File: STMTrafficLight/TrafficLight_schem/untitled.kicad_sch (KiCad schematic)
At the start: 25 parts, among them U1 74HC595D, U2 74HC595D, U3 74HC595D

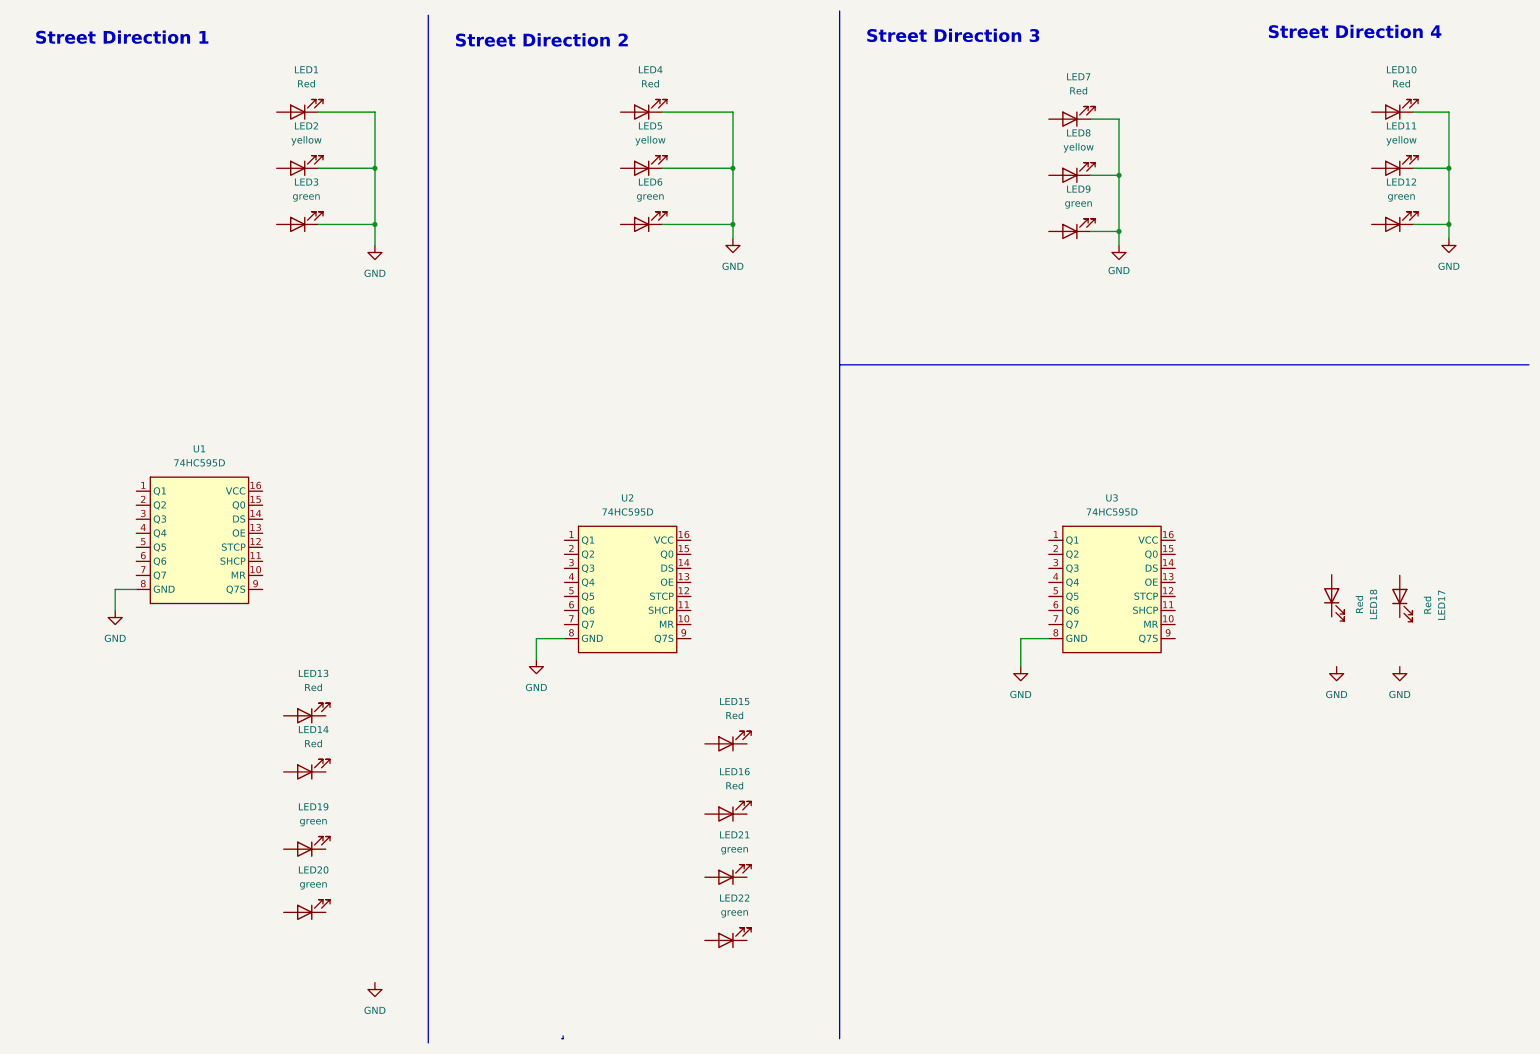
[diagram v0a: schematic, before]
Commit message: started on the traffic light shield
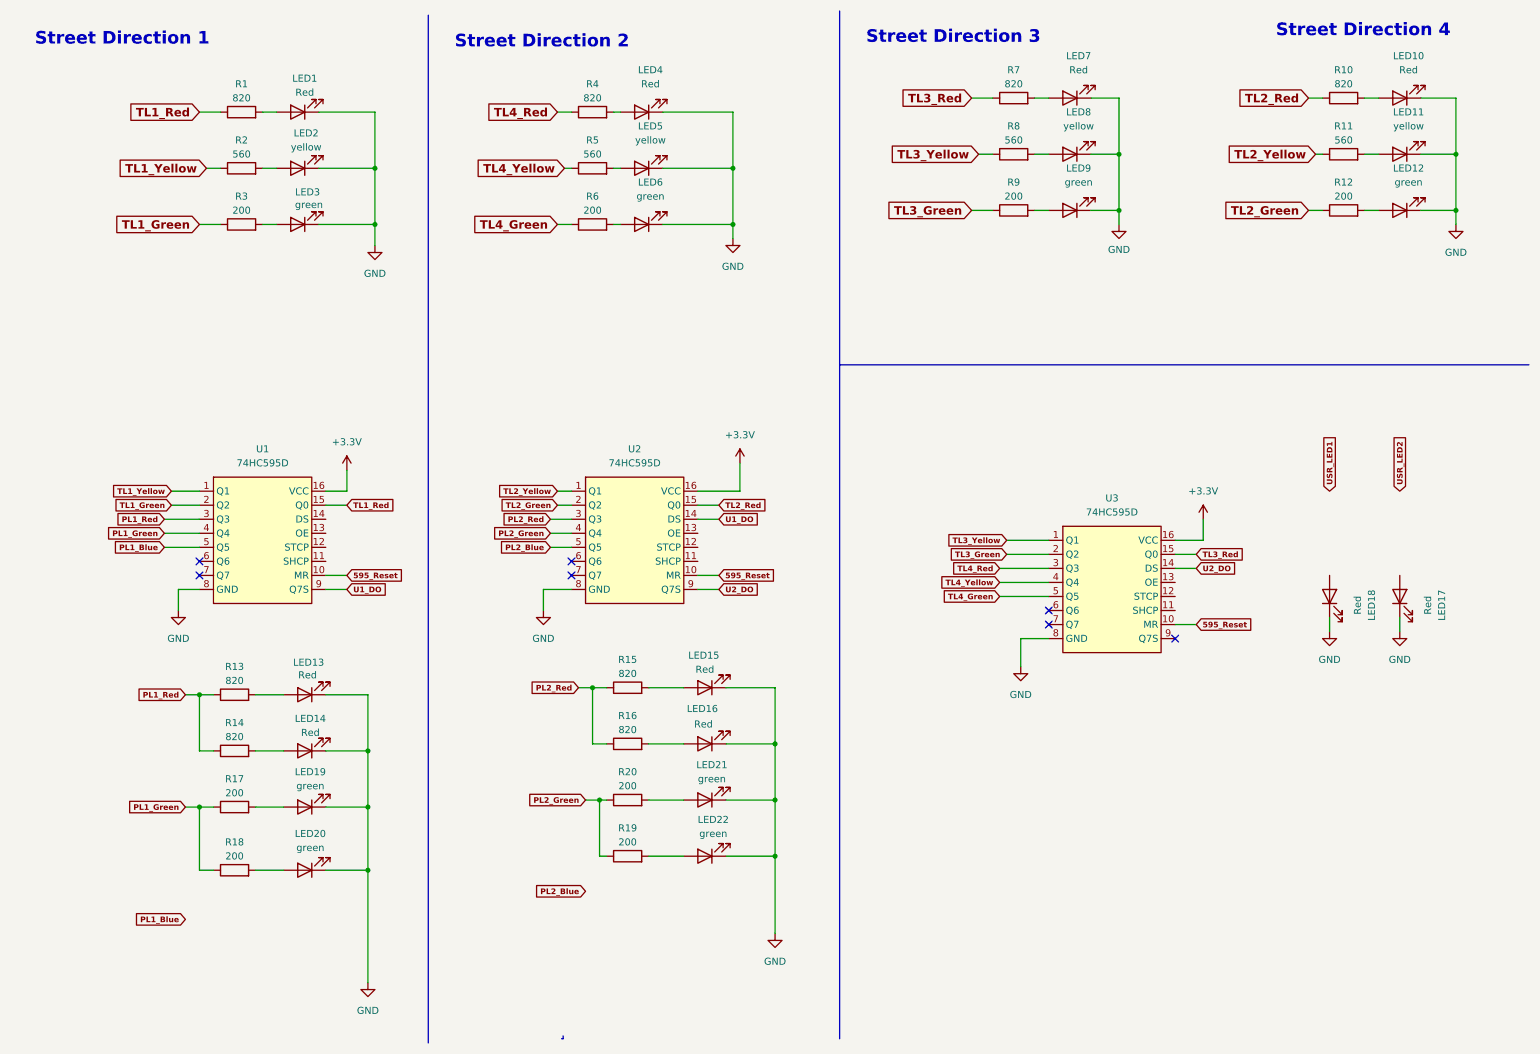
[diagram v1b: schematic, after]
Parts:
- added R1, R10, R13, R14, R15, R16, R4, R7: 820, Resistor_SMD:R_0603_1608Metric, symbol Device:R
- added R11, R2, R5, R8: 560, Resistor_SMD:R_0603_1608Metric, symbol Device:R
- added R12, R17, R18, R19, R20, R3, R6, R9: 200, Resistor_SMD:R_0603_1608Metric, symbol Device:R
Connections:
- net GND: now also LED13.1 (K), LED14.1 (K), LED15.1 (K), LED16.1 (K), LED17.1 (K), LED18.1 (K), LED19.1 (K), LED20.1 (K), LED21.1 (K), LED22.1 (K)
- net at LED15.2 (A): now also R15.2
- net TL2_Yellow: now reaches U2.1 (Q1)
- net TL2_Yellow: now also R11.1
- net 595_Reset: now reaches U2.10 (MR)
- net 595_Reset: now also U1.10 (MR), U3.10 (MR)
- net U1_DO: now reaches U2.14 (DS)
- net U1_DO: now also U1.9 (Q7S)
- net TL2_Red: now reaches U2.15 (Q0)
- net TL2_Red: now also R10.1
- net +3.3V: now reaches U2.16 (VCC)
- net +3.3V: now also U1.16 (VCC), U3.16 (VCC)
- net TL2_Green: now reaches U2.2 (Q2)
- net TL2_Green: now also R12.1
- net PL2_Red: now reaches U2.3 (Q3)
- net PL2_Red: now also R15.1, R16.1
- net PL2_Green: now reaches U2.4 (Q4)
- net PL2_Green: now also R19.1, R20.1
- net PL2_Blue: now reaches U2.5 (Q5)
- net U2_DO: now reaches U2.9 (Q7S)
- net U2_DO: now also U3.14 (DS)
- net at LED14.2 (A): now also R14.2
- net at LED10.2 (A): now also R10.2
- net at LED2.2 (A): now also R2.2
- net at LED22.2 (A): now also R19.2
- net at LED1.2 (A): now also R1.2
- net at LED3.2 (A): now also R3.2
- net at LED8.2 (A): now also R8.2
- net at LED5.2 (A): now also R5.2
- net TL3_Yellow: now reaches U3.1 (Q1)
- net TL3_Yellow: now also R8.1
- net TL3_Red: now reaches U3.15 (Q0)
- net TL3_Red: now also R7.1
- net TL3_Green: now reaches U3.2 (Q2)
- net TL3_Green: now also R9.1
- net TL4_Red: now reaches U3.3 (Q3)
- net TL4_Red: now also R4.1
- net TL4_Yellow: now reaches U3.4 (Q4)
- net TL4_Yellow: now also R5.1
- net TL4_Green: now reaches U3.5 (Q5)
- net TL4_Green: now also R6.1
- net at LED6.2 (A): now also R6.2
- net at LED19.2 (A): now also R17.2
- net at LED20.2 (A): now also R18.2
- net at LED13.2 (A): now also R13.2
- net TL1_Yellow: now reaches U1.1 (Q1)
- net TL1_Yellow: now also R2.1
- net TL1_Red: now reaches U1.15 (Q0)
- net TL1_Red: now also R1.1
- net TL1_Green: now reaches U1.2 (Q2)
- net TL1_Green: now also R3.1
- net PL1_Red: now reaches U1.3 (Q3)
- net PL1_Red: now also R13.1, R14.1
- net PL1_Green: now reaches U1.4 (Q4)
- net PL1_Green: now also R17.1, R18.1
- net PL1_Blue: now reaches U1.5 (Q5)
- net at LED12.2 (A): now also R12.2
- net at LED21.2 (A): now also R20.2
- net at LED16.2 (A): now also R16.2
- net at LED9.2 (A): now also R9.2
- net at LED4.2 (A): now also R4.2
- net at LED11.2 (A): now also R11.2
- net at LED7.2 (A): now also R7.2
- no-connect marks 0 -> 7
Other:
- moved on the sheet: LED10, LED11, LED12, LED13, LED14, LED15, LED16, LED19, LED20, LED21, LED22, LED7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

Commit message: continued on the traffic light shield
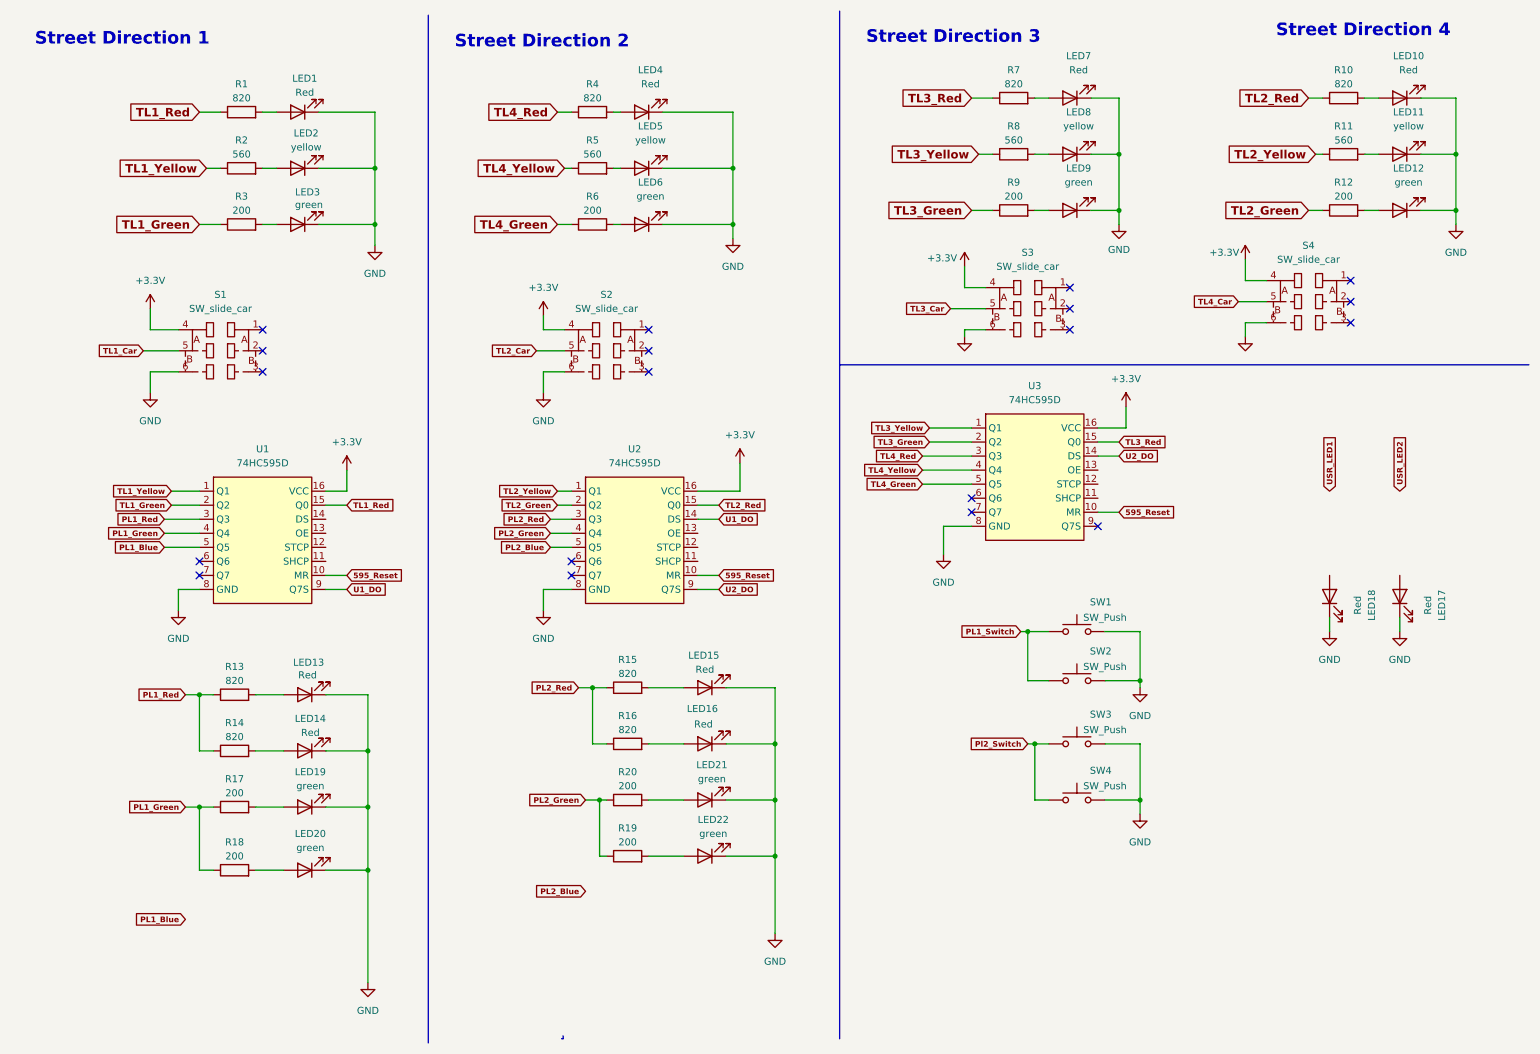
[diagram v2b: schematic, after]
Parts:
- added S1, S2, S3, S4: SW_slide_car, Trafficlight_Library:Sw_slide_car, symbol 74HC595_shiftreg_symbol:Sw_slide_car
- added SW1, SW2, SW3, SW4: SW_Push, Trafficlight_Library:sw_pedestrian_btn, symbol Switch:SW_Push
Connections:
- net +3.3V: now also S1.4, S2.4, S3.4, S4.4
- net GND: now also S1.6, S2.6, S3.6, S4.6, SW1.2, SW2.2, SW3.2, SW4.2
- new net PL1_Switch: SW1.1, SW2.1
- new net Pl2_Switch: SW3.1, SW4.1
- new net TL1_Car: S1.5
- new net TL2_Car: S2.5
- new net TL3_Car: S3.5
- new net TL4_Car: S4.5
- no-connect marks 7 -> 19
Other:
- moved on the sheet: U3

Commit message: continued on the traffic light shield
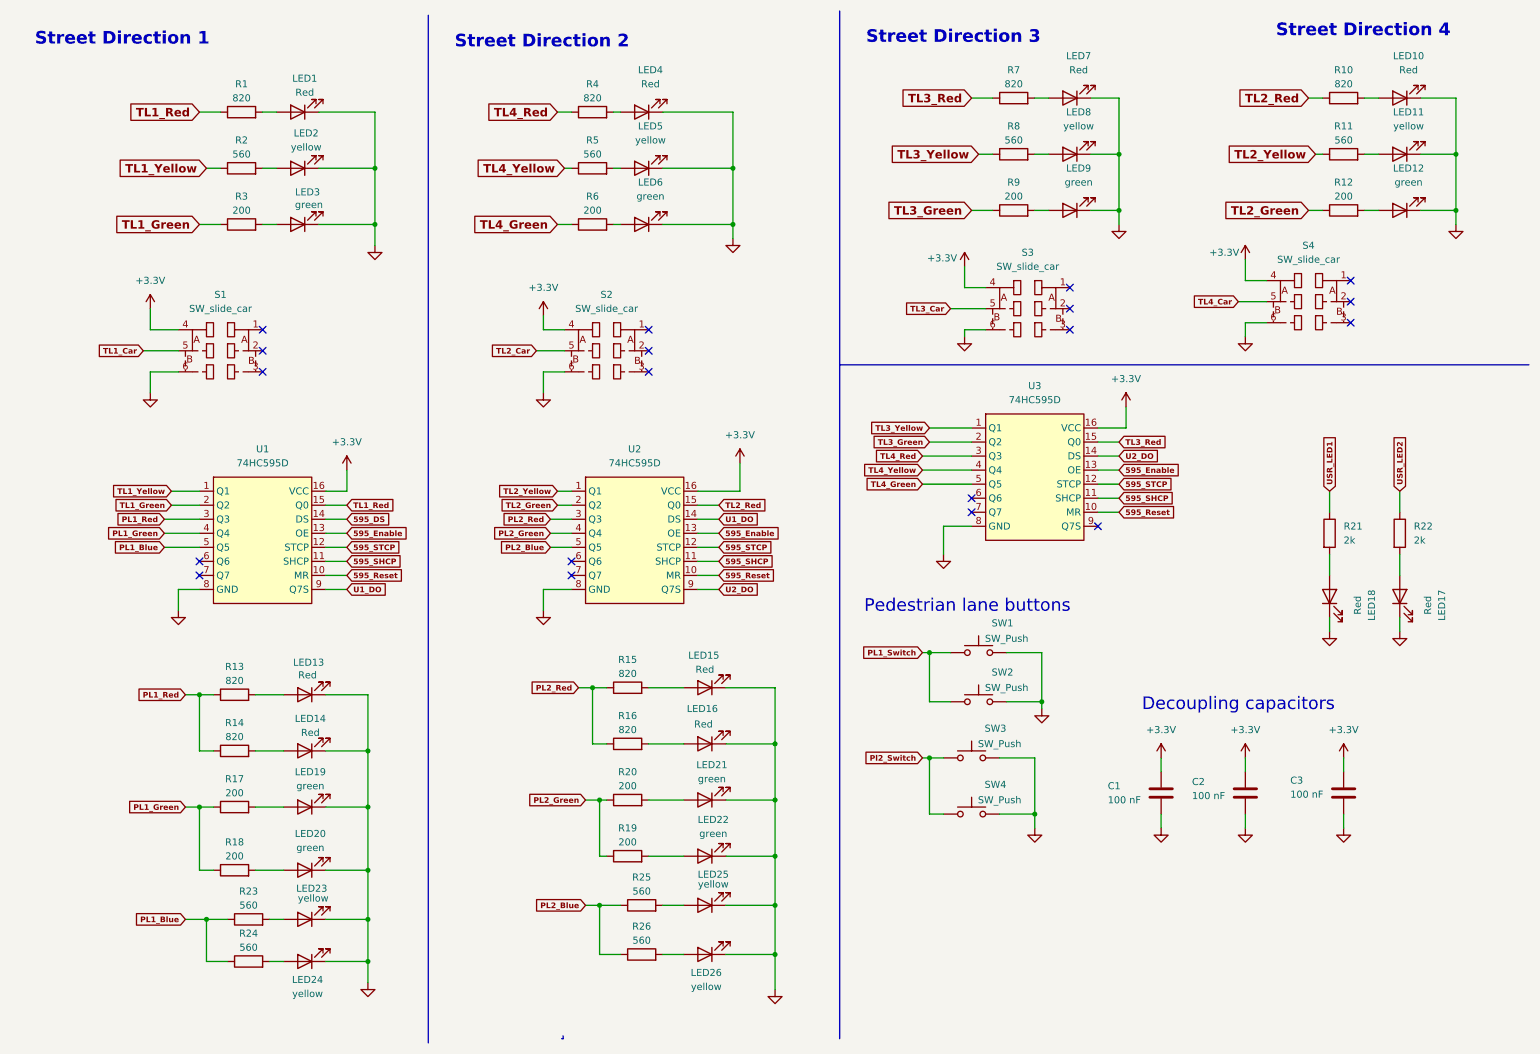
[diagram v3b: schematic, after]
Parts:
- added C1, C2, C3: 100 nF, Capacitor_SMD:C_0603_1608Metric, symbol Device:C
- added LED23, LED24, LED25, LED26: yellow, LED_SMD:LED_0805_2012Metric, symbol Device:LED
- added R21, R22: 2k, Resistor_SMD:R_0603_1608Metric, symbol Device:R
- added R23, R24, R25, R26: 560, Resistor_SMD:R_0603_1608Metric, symbol Device:R
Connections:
- net +3.3V: now also C1.1, C2.1, C3.1
- net GND: now also C1.2, C2.2, C3.2, LED23.1 (K), LED24.1 (K), LED25.1 (K), LED26.1 (K)
- net PL1_Blue: now also R23.1, R24.1
- net PL2_Blue: now also R25.1, R26.1
- net USR_LED1: now also R21.1
- net USR_LED2: now also R22.1
- net 595_SHCP: now reaches U2.11 (SHCP)
- net 595_SHCP: now also U1.11 (SHCP), U3.11 (SHCP)
- net 595_STCP: now reaches U2.12 (STCP)
- net 595_STCP: now also U1.12 (STCP), U3.12 (STCP)
- net 595_Enable: now reaches U2.13 (OE)
- net 595_Enable: now also U1.13 (OE), U3.13 (OE)
- net at LED18.2 (A): now also R21.2
- net 595_DS: now reaches U1.14 (DS)
- net at LED17.2 (A): now also R22.2
- new net: LED23.2 (A), R23.2
- new net: LED24.2 (A), R24.2
- new net: LED25.2 (A), R25.2
- new net: LED26.2 (A), R26.2
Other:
- note added: "Decoupling capacitors"
- note added: "Pedestrian lane buttons"
- title: (none) -> Traffic lights, cars, registers and switches
- moved on the sheet: SW1, SW2, SW3, SW4
